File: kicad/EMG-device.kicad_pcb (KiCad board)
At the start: 2 copper layers, 137.7 x 61.5 mm, 73 parts, among them J1 CONN_01X03, J2 Screw_Terminal_1x03, J3 Screw_Terminal_1x02, U1 AD620, U2 ATMEGA328P-PU, U3 TL072, U4 LM324N, U5 MAX1720, U6 hc-05, U7 LM1117-3.3

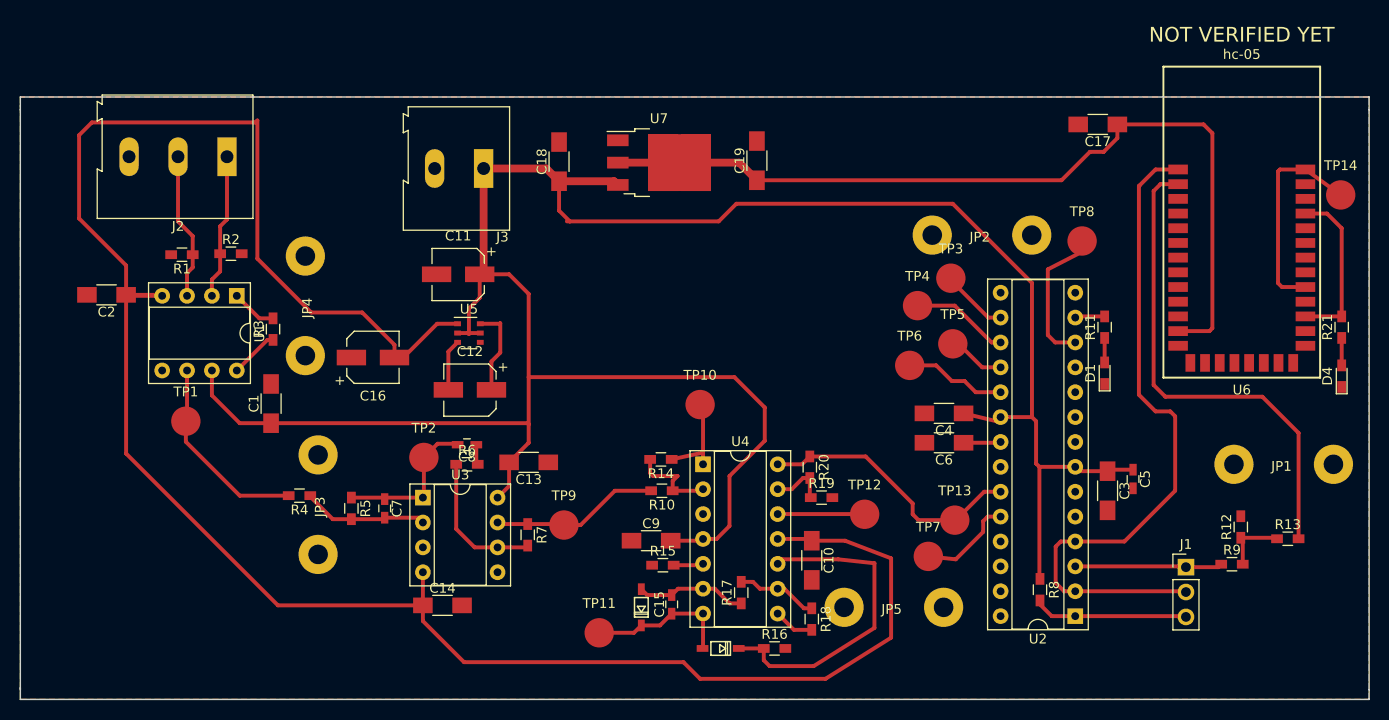
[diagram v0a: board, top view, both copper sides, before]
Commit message: wires xhanged to 0.8mil
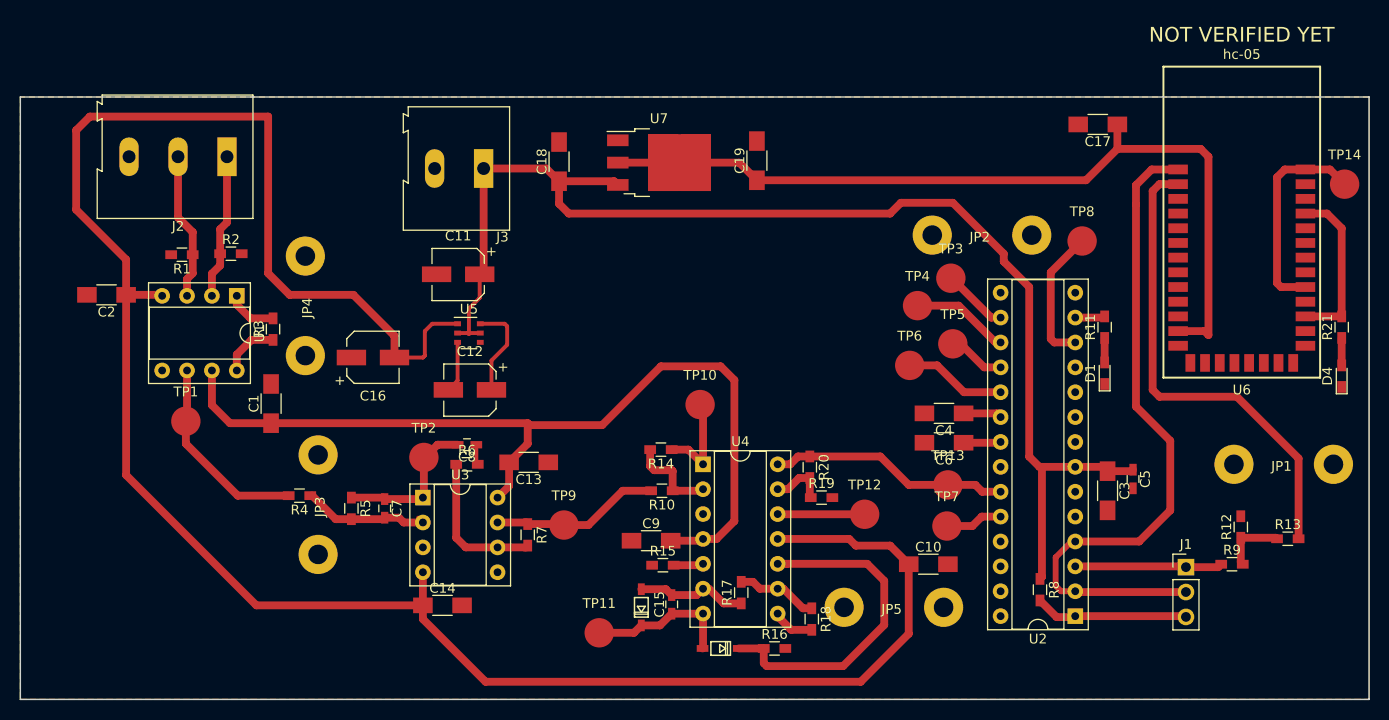
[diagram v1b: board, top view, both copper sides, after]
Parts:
- moved C10 11.9 mm to (191.9, 116.5), turned to 0 degrees
- moved TP13 3.67 mm to (193.9, 108.4)
- moved TP7 3.64 mm to (193.8, 112.6)
- moved TP14 1.17 mm to (234.4, 77.7)
- moved R14 1.00 mm to (164.6, 104.8)
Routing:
- net +5V: track 247.8 -> 226.1 mm
- net /V-: track 215.4 -> 223.3 mm
- net Net-(TP7-Pad1): track 9.85 -> 5.88 mm
- net /ADC: track 27.6 -> 24.6 mm
- net +3V3: track 88.8 -> 87.0 mm
- net Net-(D3-PadC): track 33.1 -> 34.3 mm
- net /TX3.3: track 50.2 -> 49.2 mm
- net Net-(R3-Pad1): track 4.99 -> 5.94 mm
- net Net-(C7-Pad2): track 12.8 -> 13.8 mm
- net Net-(R6-Pad1): track 14.8 -> 15.5 mm
- net Net-(C12-Pad1): track 9.23 -> 10.0 mm
- net Net-(R17-Pad2): track 8.32 -> 9.00 mm
- net Net-(TP5-Pad1): track 5.87 -> 6.47 mm
- net /RX: track 70.3 -> 69.8 mm
- net /TX: track 15.1 -> 15.6 mm
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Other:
- outline, holes or cut-outs redrawn
